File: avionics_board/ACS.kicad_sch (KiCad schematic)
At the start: 1 part

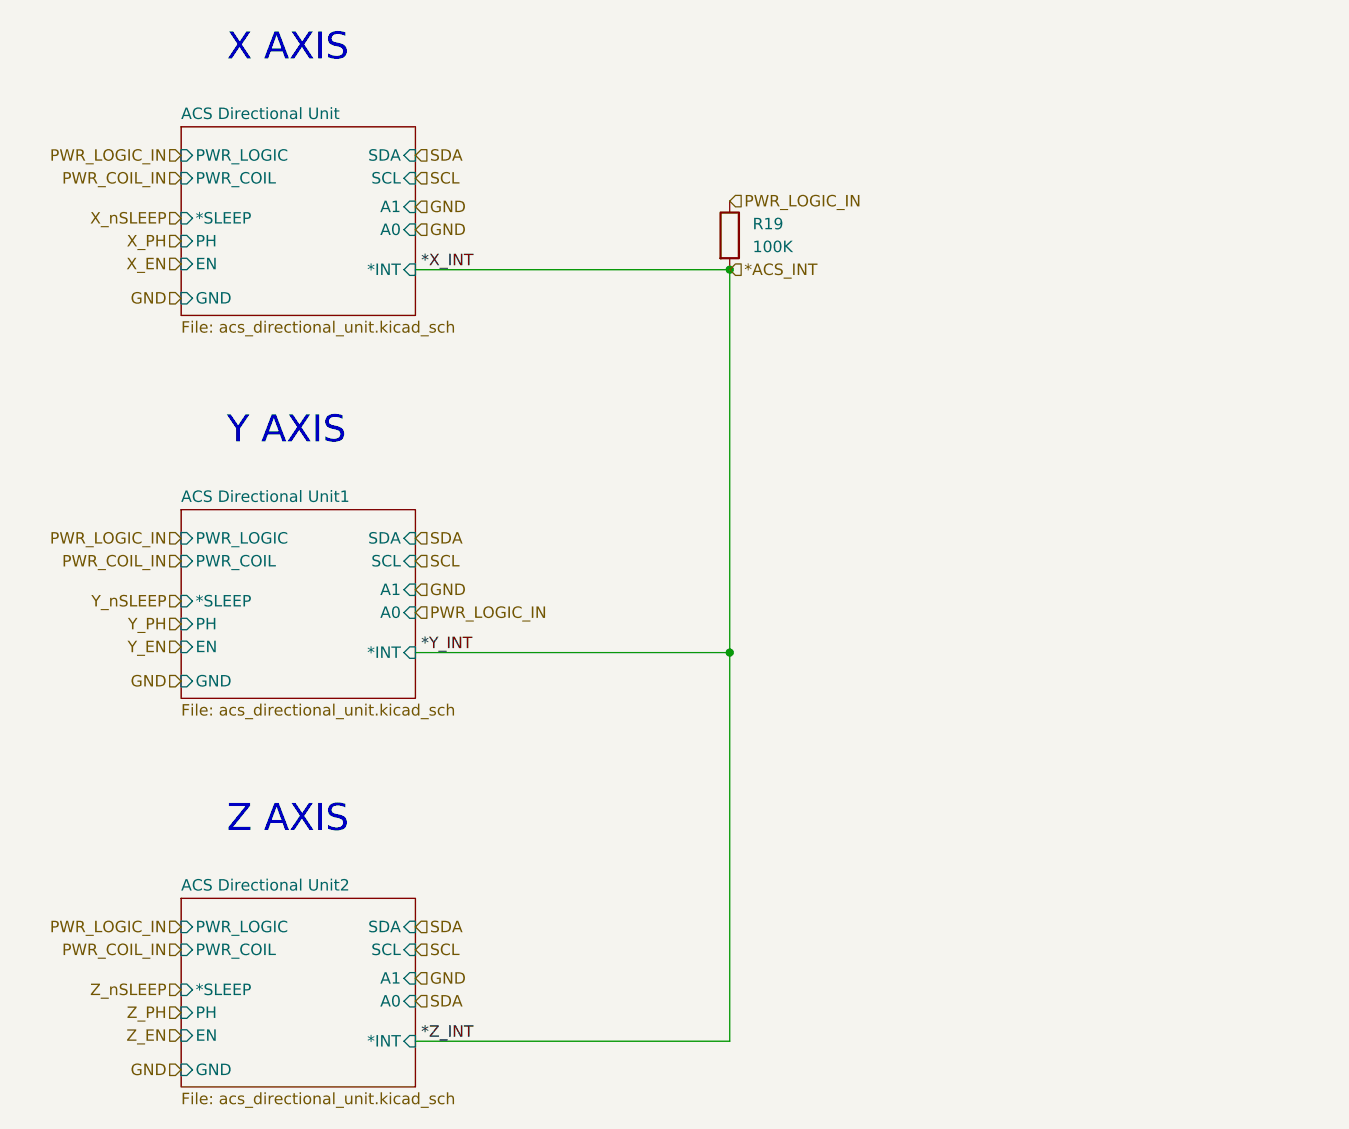
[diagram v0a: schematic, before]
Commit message: add headers for ACS and sun sensors
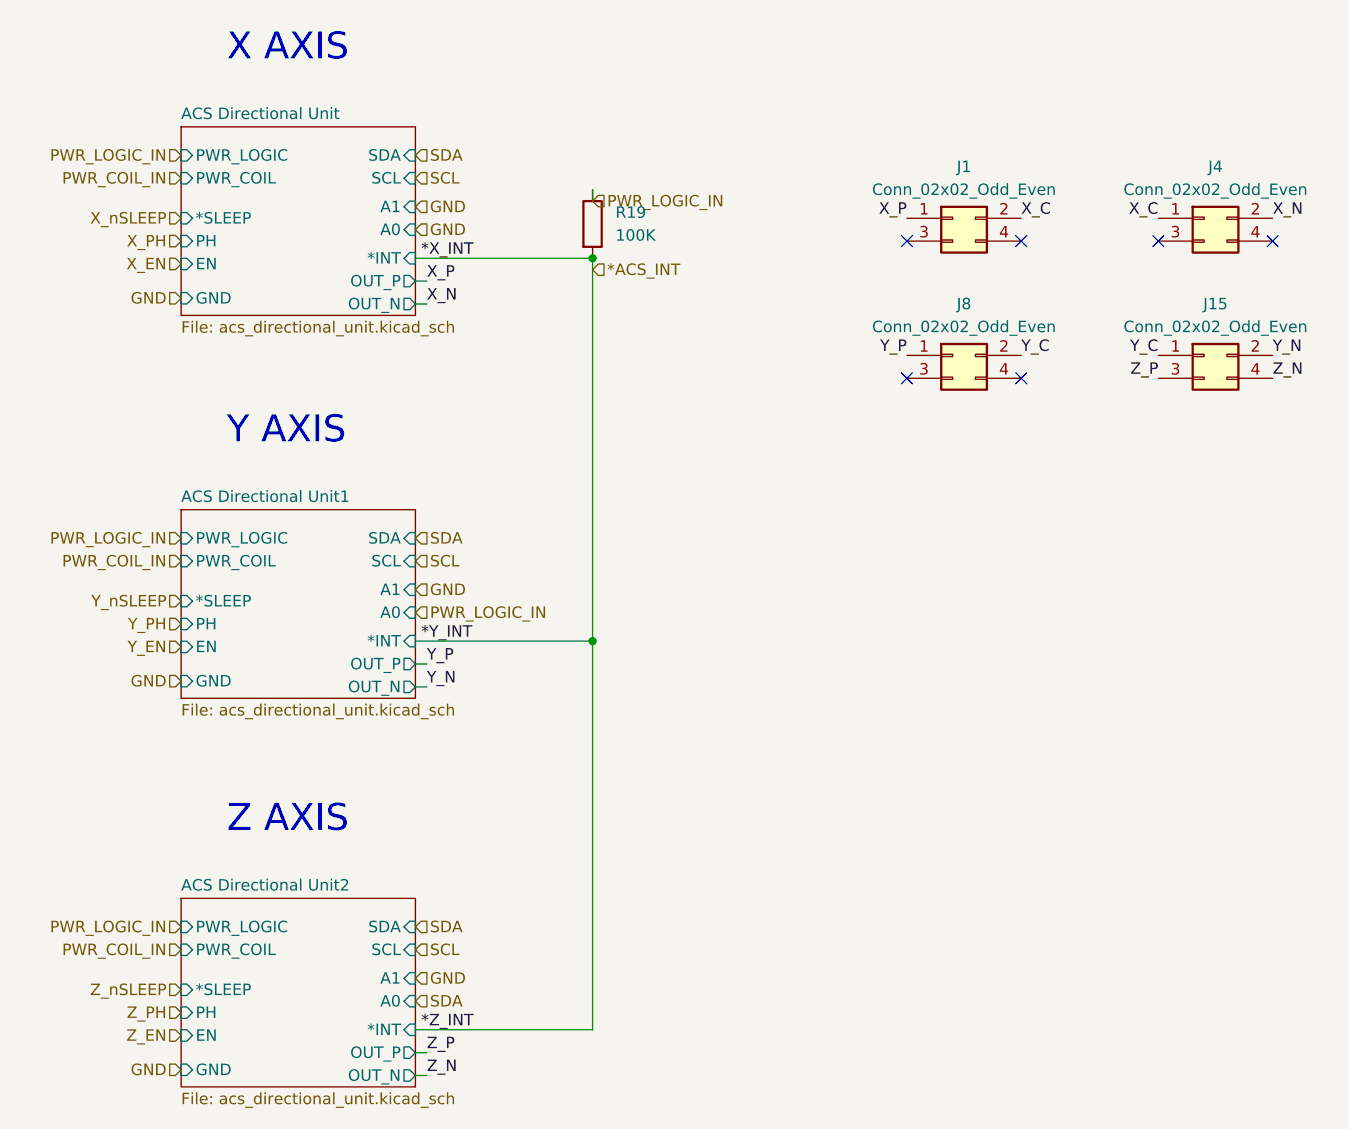
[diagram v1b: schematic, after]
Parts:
- added J1, J15, J4, J8: Conn_02x02_Odd_Even, Common:SAMTEC-CLP-102-02-X-DH, symbol Connector_Generic:Conn_02x02_Odd_Even
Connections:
- new net X_C: J1.2 (Pin_2), J4.1 (Pin_1)
- new net X_N: J4.2 (Pin_2)
- new net X_P: J1.1 (Pin_1)
- new net Y_C: J15.1 (Pin_1), J8.2 (Pin_2)
- new net Y_N: J15.2 (Pin_2)
- new net Y_P: J8.1 (Pin_1)
- new net Z_N: J15.4 (Pin_4)
- new net Z_P: J15.3 (Pin_3)
- no-connect marks 0 -> 6
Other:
- sheet ACS Directional Unit ports: added OUT_N, OUT_P; removed none
- sheet ACS Directional Unit1 ports: added OUT_N, OUT_P; removed none
- sheet ACS Directional Unit2 ports: added OUT_N, OUT_P; removed none
- moved on the sheet: R19

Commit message: use SAMTEC connectors for AVI to side panels, try HARWIN ones next
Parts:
- renumbered J4 to J2, J8 to J3, J15 to J4, R19 to R20
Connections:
- net X_N: now also J1.2 (Pin_2), J1.4 (Pin_4), J2.4 (Pin_4)
- net X_P: now also J1.3 (Pin_3), J2.1 (Pin_1), J2.3 (Pin_3)
- net Y_N: now also J3.2 (Pin_2), J3.4 (Pin_4), J4.4 (Pin_4)
- net Y_P: now also J3.3 (Pin_3), J4.1 (Pin_1), J4.3 (Pin_3)
- net Z_N: no longer J4.4 (Pin_4)
- net Z_P: no longer J4.3 (Pin_3)
- removed net X_C: J1.2 (Pin_2), J2.1 (Pin_1)
- removed net Y_C: J3.2 (Pin_2), J4.1 (Pin_1)
- no-connect marks 6 -> 0
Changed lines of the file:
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@@
 		(color 0 0 0 0)
-	)
-	(no_connect
-		(at 192.405 65.405)
-	)
-	(no_connect
-		(at 151.765 80.645)
-	)
-	(no_connect
-		(at 164.465 65.405)
-	)
-	(no_connect
-		(at 151.765 65.405)
-	)
-	(no_connect
-		(at 179.705 65.405)
-	)
-	(no_connect
-		(at 164.465 80.645)
 	)
 	(wire
@@
 		)
 	)
-	(label "Y_C"
+	(label "Y_N"
 		(at 164.465 78.105 0)
 		(fields_autoplaced yes)
@@
 		)
 	)
-	(label "Z_P"
-		(at 98.425 155.575 0)
-		(fields_autoplaced yes)
-		(effects
-			(font
-				(size 1.27 1.27)
-			)
-			(justify left bottom)
-		)
-	)
-	(label "Z_N"
-		(at 98.425 158.115 0)
+	(label "Y_N"
+		(at 192.405 80.645 0)
 		(fields_autoplaced yes)
 		(effects
@@
 		)
 	)
-	(label "Z_N"
-		(at 192.405 80.645 0)
-		(fields_autoplaced yes)
-		(effects
-			(font
-				(size 1.27 1.27)
-			)
-			(justify left bottom)
-		)
-	)
-	(label "X_C"
+	(label "X_P"
 		(at 179.705 62.865 180)
 		(fields_autoplaced yes)
@@
 		)
 	)
-	(label "Y_C"
+	(label "Y_P"
 		(at 179.705 78.105 180)
 		(fields_autoplaced yes)
@@
 		)
 	)
+	(label "Y_P"
+		(at 179.705 80.645 180)
+		(fields_autoplaced yes)
+		(effects
+			(font
+				(size 1.27 1.27)
+			)
+			(justify right bottom)
+		)
+	)
 	(label "Y_N"
 		(at 98.425 114.935 0)
@@
 	)
 	(label "Y_N"
+		(at 164.465 80.645 0)
+		(fields_autoplaced yes)
+		(effects
+			(font
+				(size 1.27 1.27)
+			)
+			(justify left bottom)
+		)
+	)
+	(label "Y_P"
+		(at 151.765 80.645 180)
+		(fields_autoplaced yes)
+		(effects
+			(font
+				(size 1.27 1.27)
+			)
+			(justify right bottom)
+		)
+	)
+	(label "Y_N"
 		(at 192.405 78.105 0)
 		(fields_autoplaced yes)
@@
 		)
 	)
+	(label "X_P"
+		(at 179.705 65.405 180)
+		(fields_autoplaced yes)
+		(effects
+			(font
+				(size 1.27 1.27)
+			)
+			(justify right bottom)
+		)
+	)
 	(label "*Z_INT"
 		(at 97.79 153.035 0)
@@
 		)
 	)
-	(label "X_C"
+	(label "X_N"
 		(at 164.465 62.865 0)
 		(fields_autoplaced yes)
@@
 		)
 	)
-	(label "Z_P"
-		(at 179.705 80.645 180)
-		(fields_autoplaced yes)
-		(effects
-			(font
-				(size 1.27 1.27)
-			)
-			(justify right bottom)
+	(label "X_N"
+		(at 164.465 65.405 0)
+		(fields_autoplaced yes)
+		(effects
+			(font
+				(size 1.27 1.27)
+			)
+			(justify left bottom)
 		)
 	)
@@
 		)
 	)
+	(label "X_N"
+		(at 192.405 65.405 0)
+		(fields_autoplaced yes)
+		(effects
+			(font
+				(size 1.27 1.27)
+			)
+			(justify left bottom)
+		)
+	)
 	(label "*X_INT"
 		(at 97.79 67.31 0)
@@
 			)
 			(justify left bottom)
+		)
+	)
+	(label "X_P"
+		(at 151.765 65.405 180)
+		(fields_autoplaced yes)
+		(effects
+			(font
+				(size 1.27 1.27)
+			)
+			(justify right bottom)
+		)
+	)
+	(global_label "Z_P"
+		(shape input)
+		(at 98.425 155.575 0)
+		(fields_autoplaced yes)
+		(effects
+			(font
+				(size 1.27 1.27)
+			)
+			(justify left)
+		)
+		(property "Intersheetrefs" "${INTERSHEET_REFS}"
+			(at 104.8573 155.575 0)
+			(effects
+				(font
+					(size 1.27 1.27)
+				)
+				(justify left)
+				(hide yes)
+			)
+		)
+	)
+	(global_label "Z_N"
+		(shape input)
+		(at 98.425 158.115 0)
+		(fields_autoplaced yes)
+		(effects
+			(font
+				(size 1.27 1.27)
+			)
+			(justify left)
+		)
+		(property "Intersheetrefs" "${INTERSHEET_REFS}"
+			(at 104.9178 158.115 0)
+			(effects
+				(font
+					(size 1.27 1.27)
+				)
+				(justify left)
+				(hide yes)
+			)
 		)
 	)
@@
 		(dnp no)
 		(fields_autoplaced yes)
-		(property "Reference" "J8"
+		(property "Reference" "J3"
 			(at 158.115 72.39 0)
 			(effects
@@
 			(project "AVIONICS_BOARD"
 				(path "/f6cc00ab-17f1-4973-862f-7ac95fe70668/1f9ae17d-3f3e-4633-9b01-30c344473415"
-					(reference "J8")
+					(reference "J3")
 					(unit 1)
 				)
@@
 		(dnp no)
 		(fields_autoplaced yes)
-		(property "Reference" "R19"
+		(property "Reference" "R20"
 			(at 119.38 62.2299 0)
 			(effects
@@
 			(project "AVIONICS_BOARD"
 				(path "/f6cc00ab-17f1-4973-862f-7ac95fe70668/1f9ae17d-3f3e-4633-9b01-30c344473415"
-					(reference "R19")
+					(reference "R20")
 					(unit 1)
 				)
@@
 		(dnp no)
 		(fields_autoplaced yes)
-		(property "Reference" "J4"
+		(property "Reference" "J2"
 			(at 186.055 57.15 0)
 			(effects
@@
 			(project "AVIONICS_BOARD"
 				(path "/f6cc00ab-17f1-4973-862f-7ac95fe70668/1f9ae17d-3f3e-4633-9b01-30c344473415"
-					(reference "J4")
+					(reference "J2")
 					(unit 1)
 				)
@@
 		(dnp no)
 		(fields_autoplaced yes)
-		(property "Reference" "J15"
+		(property "Reference" "J4"
 			(at 186.055 72.39 0)
 			(effects
@@
 			(project "AVIONICS_BOARD"
 				(path "/f6cc00ab-17f1-4973-862f-7ac95fe70668/1f9ae17d-3f3e-4633-9b01-30c344473415"
-					(reference "J15")
+					(reference "J4")
 					(unit 1)
 				)
